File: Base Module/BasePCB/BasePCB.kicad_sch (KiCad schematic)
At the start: 1 part

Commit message: Added to schematic
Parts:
- added C? (x2): 22pF, symbol Device:C_Small
- added C?: 10uF, symbol Device:C_Small
- added C? (x3): 0.1uF, symbol Device:C_Small
- added C?: 1uF, symbol Device:C_Small
- added R?: 10k, symbol Device:R_Small
- added R? (x2): 22, symbol Device:R_Small
- added SW?: SW_Push, symbol Switch:SW_Push
- added Y?: Crystal_GND24_Small, symbol Device:Crystal_GND24_Small
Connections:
- net +5V: now also U?.7 (VBUS), C?.1, C?.1, C?.1, C?.1
- net GND: now also C?.1, C?.2, C?.2, C?.2, C?.2, C?.2, C?.2, R?.2, SW?.1, Y?.2, Y?.4
- net at U?.13 (~{RESET}): now also SW?.2
- net at U?.16 (XTAL2): now also C?.2, Y?.3
- net at U?.17 (XTAL1): now also C?.1, Y?.1
- net at U?.3 (D-): now also R?.2
- net at U?.33 (~{HWB}/PE2): now also R?.1
- net at U?.4 (D+): now also R?.2
- net at U?.6 (UCAP): now also C?.1

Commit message: Finished microcontroller
On schematic
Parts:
- added R?: 10k, symbol Device:R_Small
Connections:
- net +5V: now also R?.1
- net at SW?.2, U?.13 (~{RESET}): now also R?.2
- net D+: now reaches R?.1
- net D-: now reaches R?.1
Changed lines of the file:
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@@
   (junction (at 49.53 140.97) (diameter 0) (color 0 0 0 0)
   )
+  (junction (at 73.66 72.39) (diameter 0) (color 0 0 0 0)
+  )
   (junction (at 55.88 82.55) (diameter 0) (color 0 0 0 0)
   )
@@
     (stroke (width 0) (type default) (color 0 0 0 0))
   )
+  (wire (pts (xy 73.66 66.04) (xy 73.66 72.39))
+    (stroke (width 0) (type default) (color 0 0 0 0))
+  )
   (wire (pts (xy 60.96 100.33) (xy 76.2 100.33))
     (stroke (width 0) (type default) (color 0 0 0 0))
@@
     (stroke (width 0) (type default) (color 0 0 0 0))
   )
+  (wire (pts (xy 73.66 58.42) (xy 73.66 60.96))
+    (stroke (width 0) (type default) (color 0 0 0 0))
+  )
   (wire (pts (xy 43.18 74.93) (xy 43.18 86.36))
     (stroke (width 0) (type default) (color 0 0 0 0))
@@
     (stroke (width 0) (type default) (color 0 0 0 0))
   )
-  (wire (pts (xy 68.58 72.39) (xy 76.2 72.39))
+  (wire (pts (xy 73.66 72.39) (xy 76.2 72.39))
+    (stroke (width 0) (type default) (color 0 0 0 0))
+  )
+  (wire (pts (xy 68.58 72.39) (xy 73.66 72.39))
     (stroke (width 0) (type default) (color 0 0 0 0))
   )
@@
   (wire (pts (xy 67.31 105.41) (xy 67.31 107.95))
     (stroke (width 0) (type default) (color 0 0 0 0))
+  )
+  (global_label "D-" (shape input) (at 45.72 100.33 180) (fields_autoplaced)
+    (effects (font (size 1.27 1.27)) (justify right))
+    (property "Intersheet References" "${INTERSHEET_REFS}" (id 0) (at 40.4645 100.2506 0)
+      (effects (font (size 1.27 1.27)) (justify right) hide)
+    )
+  )
+  (global_label "D+" (shape input) (at 45.72 97.79 180) (fields_autoplaced)
+    (effects (font (size 1.27 1.27)) (justify right))
+    (property "Intersheet References" "${INTERSHEET_REFS}" (id 0) (at 40.4645 97.7106 0)
+      (effects (font (size 1.27 1.27)) (justify right) hide)
+    )
   )
   (symbol (lib_id "power:GND") (at 43.18 90.17 0) (unit 1)
@@
     )
     (property "Datasheet" "" (id 3) (at 53.34 68.58 0)
+      (effects (font (size 1.27 1.27)) hide)
+    )
+    (pin "1")
+  )
+  (symbol (lib_id "Device:R_Small") (at 73.66 63.5 0) (unit 1)
+    (in_bom yes) (on_board yes) (fields_autoplaced)
+    (property "Reference" "R?" (id 0) (at 76.2 62.2299 0)
+      (effects (font (size 1.27 1.27)) (justify left))
+    )
+    (property "Value" "10k" (id 1) (at 76.2 64.7699 0)
+      (effects (font (size 1.27 1.27)) (justify left))
+    )
+    (property "Footprint" "" (id 2) (at 73.66 63.5 0)
+      (effects (font (size 1.27 1.27)) hide)
+    )
+    (property "Datasheet" "~" (id 3) (at 73.66 63.5 0)
+      (effects (font (size 1.27 1.27)) hide)
+    )
+    (pin "1")
+    (pin "2")
+  )
+  (symbol (lib_id "power:+5V") (at 73.66 58.42 0) (unit 1)
+    (in_bom yes) (on_board yes) (fields_autoplaced)
+    (property "Reference" "#PWR?" (id 0) (at 73.66 62.23 0)
+      (effects (font (size 1.27 1.27)) hide)
+    )
+    (property "Value" "+5V" (id 1) (at 73.66 53.34 0))
+    (property "Footprint" "" (id 2) (at 73.66 58.42 0)
+      (effects (font (size 1.27 1.27)) hide)
+    )
+    (property "Datasheet" "" (id 3) (at 73.66 58.42 0)
       (effects (font (size 1.27 1.27)) hide)
     )
@@
       (reference "#PWR?") (unit 1) (value "GND") (footprint "")
     )
+    (path "/9f1cfdcb-9cfa-46ab-8989-5487559cd9c0"
+      (reference "#PWR?") (unit 1) (value "+5V") (footprint "")
+    )
     (path "/e7daf409-0e3e-4c86-8152-279ed084cab6"
       (reference "#PWR?") (unit 1) (value "GND") (footprint "")
@@
       (reference "R?") (unit 1) (value "22") (footprint "")
     )
+    (path "/9b480758-32ee-458e-8ad1-37bc16b26dc3"
+      (reference "R?") (unit 1) (value "10k") (footprint "")
+    )
     (path "/a96590dc-4d23-4d27-98c2-fd596df790b7"

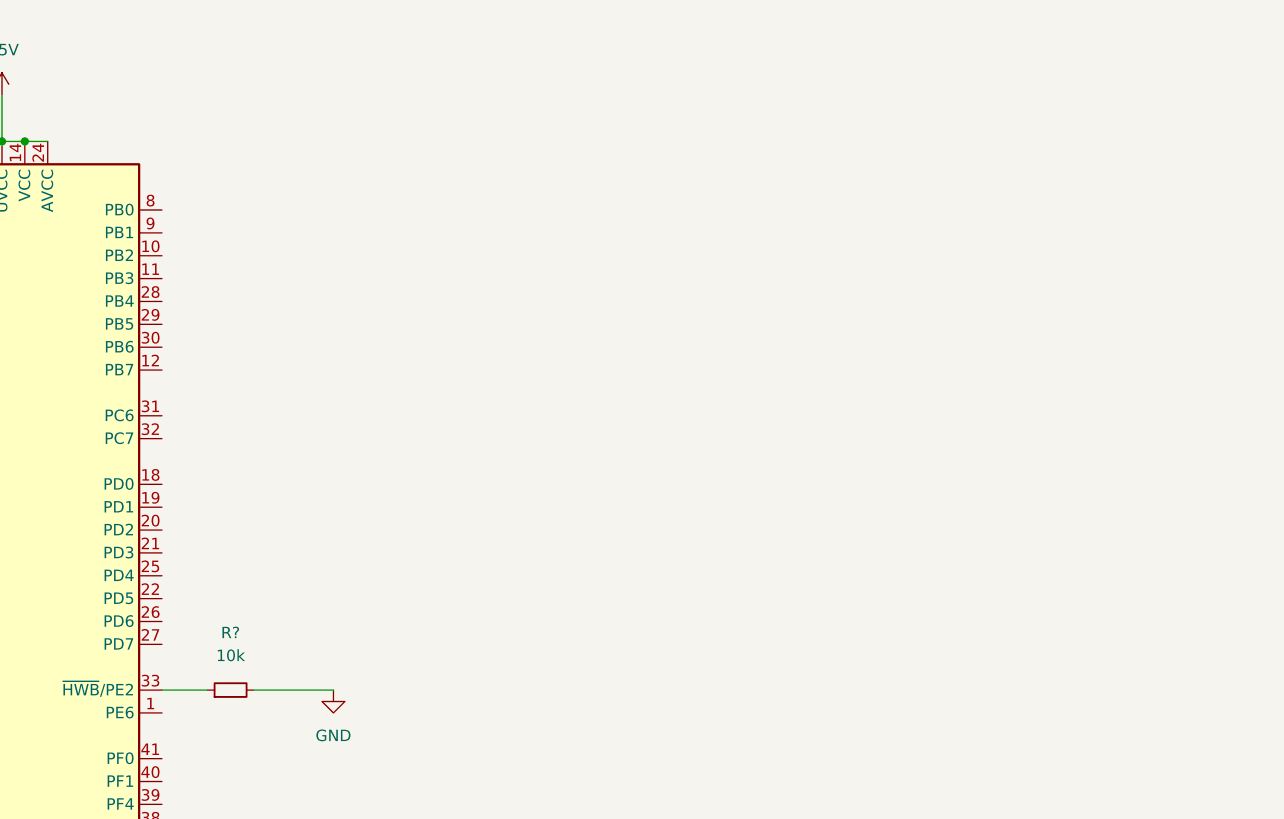
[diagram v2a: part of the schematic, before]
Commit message: Added switch matrix and USB
not sure about USB A, might need to edit later
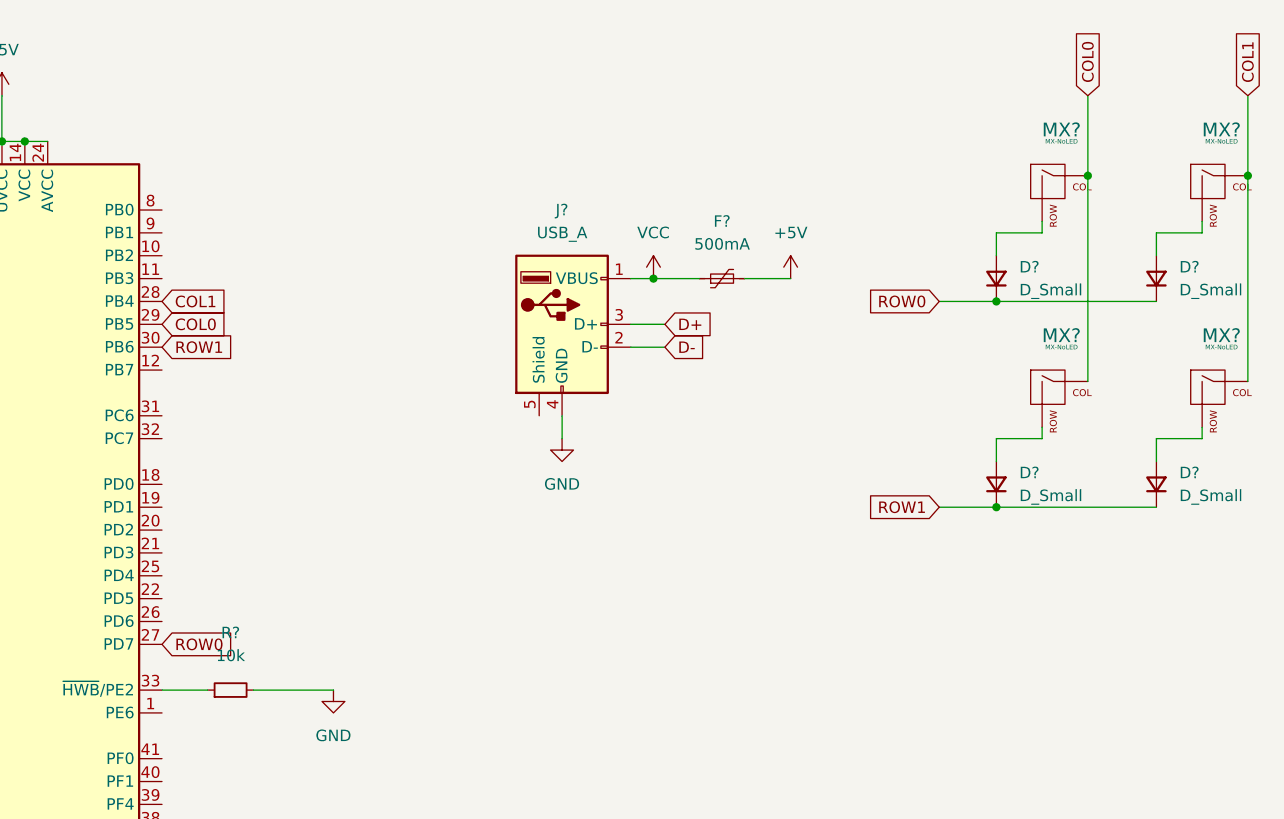
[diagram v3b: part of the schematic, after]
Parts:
- added D? (x4): D_Small, symbol Device:D_Small
- added F?: 500mA, symbol Device:Polyfuse_Small
- added J?: USB_A, symbol Connector:USB_A
- added MX? (x4): MX-NoLED, symbol MX_Alps_Hybrid:MX-NoLED
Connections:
- net +5V: now also F?.2
- net D+: now also J?.3 (D+)
- net D-: now also J?.2 (D-)
- net GND: now also J?.4 (GND)
- net ROW0: now reaches U?.27 (PD7)
- net ROW0: now also D?.1 (K), D?.1 (K)
- net COL1: now reaches U?.28 (PB4)
- net COL1: now also MX?.1 (COL), MX?.1 (COL)
- net COL0: now reaches U?.29 (PB5)
- net COL0: now also MX?.1 (COL), MX?.1 (COL)
- net ROW1: now reaches U?.30 (PB6)
- net ROW1: now also D?.1 (K), D?.1 (K)
- new net: D?.2 (A), MX?.2 (ROW) (x4)
- new net VCC: F?.1, J?.1 (VBUS)

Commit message: Added and assigned footprints
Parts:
- C1, C2, C3, C4, C5, C6, C7: renamed from C?; footprint (none) -> Capacitor_SMD:C_0805_2012Metric
- D1, D2, D3, D4: renamed from D?; footprint (none) -> Diode_SMD:D_SOD-123
- F1: renamed from F?; footprint (none) -> Fuse:Fuse_1206_3216Metric
- J1: renamed from J?; footprint (none) -> random-keyboard-parts:USB-A-Generic
- MX1, MX2, MX3, MX4: renamed from MX?; footprint (none) -> MX_Alps_Hybrid:MX-1U-NoLED
- R1, R2, R3, R4: renamed from R?; footprint (none) -> Resistor_SMD:R_0805_2012Metric
- SW1: renamed from SW?; footprint (none) -> random-keyboard-parts:SKQG-1155865
- Y1: renamed from Y?; footprint (none) -> Crystal:Crystal_SMD_3225-4Pin_3.2x2.5mm
- gave numbers to parts that had none: 1

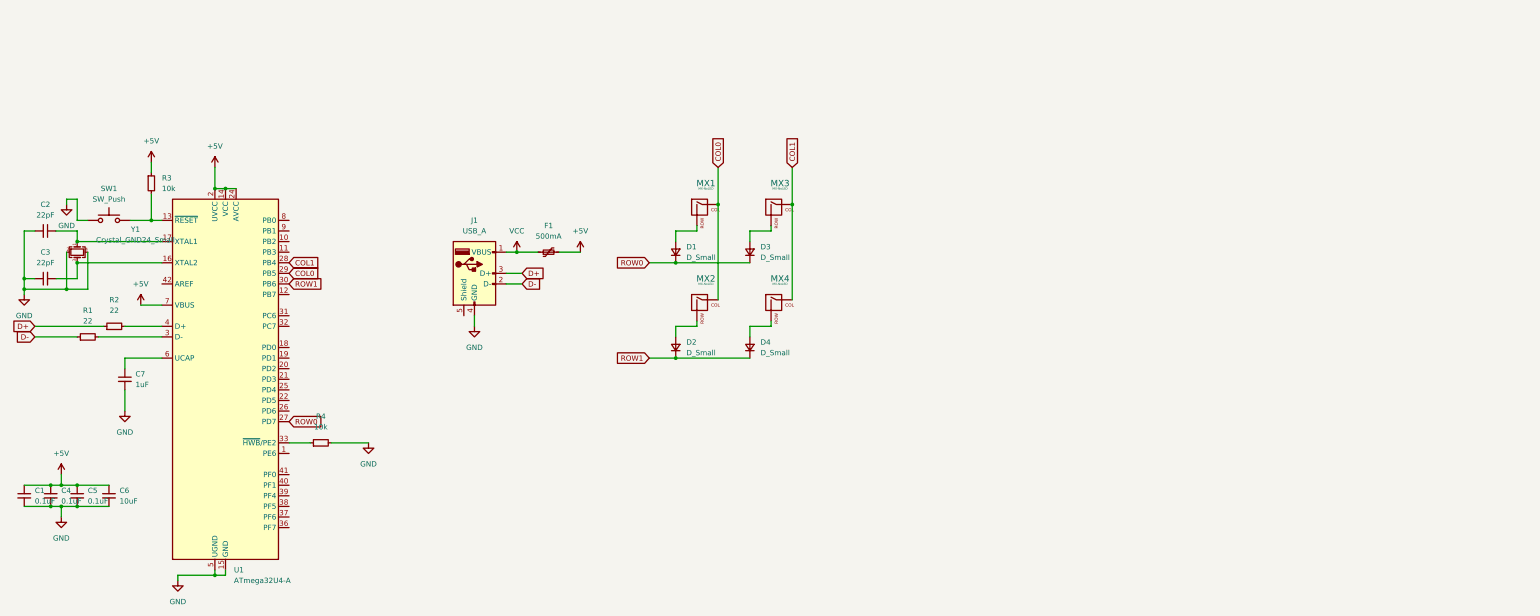
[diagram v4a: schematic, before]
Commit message: Updated schematic
Added rest of keys to schematic
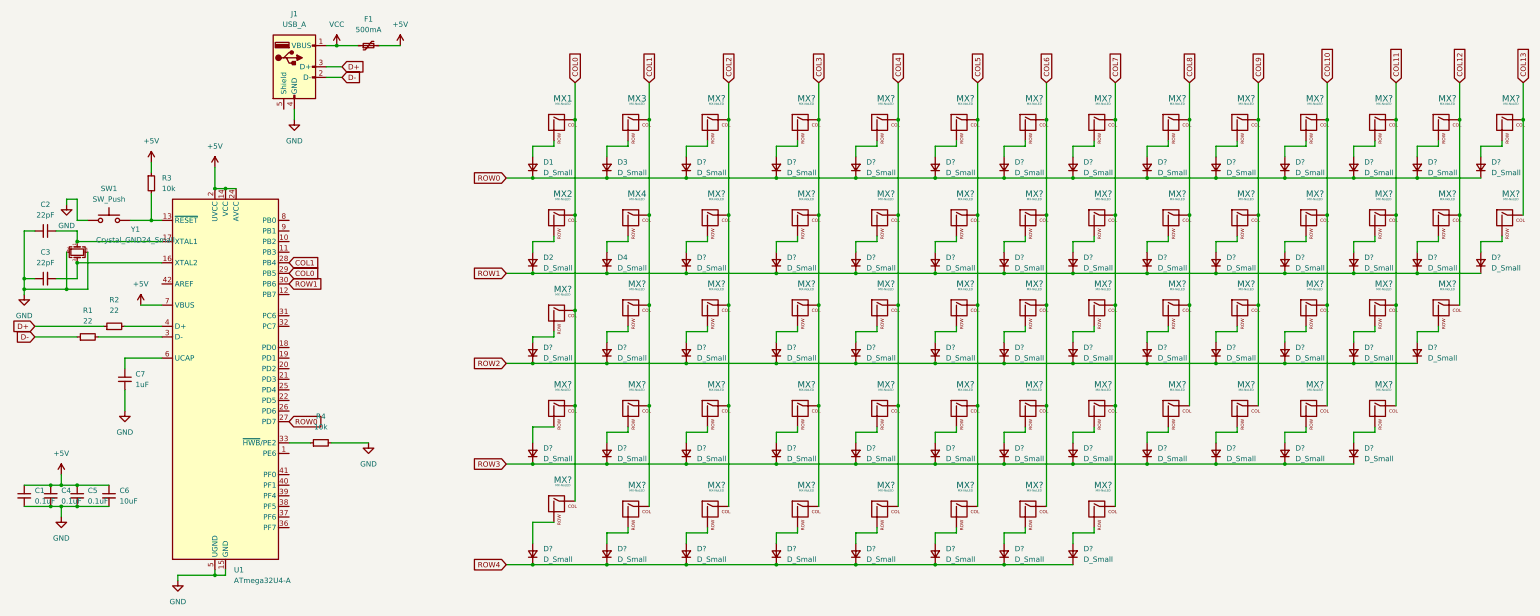
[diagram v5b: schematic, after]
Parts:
- added D? (x57): D_Small, Diode_SMD:D_SOD-123, symbol Device:D_Small
- added MX? (x57): MX-NoLED, MX_Alps_Hybrid:MX-1U-NoLED, symbol MX_Alps_Hybrid:MX-NoLED
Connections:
- net COL0: now also MX?.1 (COL), MX?.1 (COL), MX?.1 (COL)
- net COL1: now also MX?.1 (COL), MX?.1 (COL), MX?.1 (COL)
- net ROW0: now also D?.1 (K), D?.1 (K), D?.1 (K), D?.1 (K), D?.1 (K), D?.1 (K), D?.1 (K), D?.1 (K), D?.1 (K), D?.1 (K), D?.1 (K), D?.1 (K)
- net ROW1: now also D?.1 (K), D?.1 (K), D?.1 (K), D?.1 (K), D?.1 (K), D?.1 (K), D?.1 (K), D?.1 (K), D?.1 (K), D?.1 (K), D?.1 (K), D?.1 (K)
- new net: D?.2 (A), MX?.2 (ROW) (x57)
- new net COL10: MX?.1 (COL), MX?.1 (COL), MX?.1 (COL), MX?.1 (COL)
- new net COL11: MX?.1 (COL), MX?.1 (COL), MX?.1 (COL), MX?.1 (COL)
- new net COL12: MX?.1 (COL), MX?.1 (COL), MX?.1 (COL)
- new net COL13: MX?.1 (COL), MX?.1 (COL)
- new net COL2: MX?.1 (COL), MX?.1 (COL), MX?.1 (COL), MX?.1 (COL), MX?.1 (COL)
- new net COL3: MX?.1 (COL), MX?.1 (COL), MX?.1 (COL), MX?.1 (COL), MX?.1 (COL)
- new net COL4: MX?.1 (COL), MX?.1 (COL), MX?.1 (COL), MX?.1 (COL), MX?.1 (COL)
- new net COL5: MX?.1 (COL), MX?.1 (COL), MX?.1 (COL), MX?.1 (COL), MX?.1 (COL)
- new net COL6: MX?.1 (COL), MX?.1 (COL), MX?.1 (COL), MX?.1 (COL), MX?.1 (COL)
- new net COL7: MX?.1 (COL), MX?.1 (COL), MX?.1 (COL), MX?.1 (COL), MX?.1 (COL)
- new net COL8: MX?.1 (COL), MX?.1 (COL), MX?.1 (COL), MX?.1 (COL)
- new net COL9: MX?.1 (COL), MX?.1 (COL), MX?.1 (COL), MX?.1 (COL)
- new net ROW2: D?.1 (K), D?.1 (K), D?.1 (K), D?.1 (K), D?.1 (K), D?.1 (K), D?.1 (K), D?.1 (K), D?.1 (K), D?.1 (K), D?.1 (K), D?.1 (K), D?.1 (K)
- new net ROW3: D?.1 (K), D?.1 (K), D?.1 (K), D?.1 (K), D?.1 (K), D?.1 (K), D?.1 (K), D?.1 (K), D?.1 (K), D?.1 (K), D?.1 (K), D?.1 (K)
- new net ROW4: D?.1 (K), D?.1 (K), D?.1 (K), D?.1 (K), D?.1 (K), D?.1 (K), D?.1 (K), D?.1 (K)
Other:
- moved on the sheet: D1, D2, D3, D4, F1, J1, MX1, MX2, MX3, MX4
